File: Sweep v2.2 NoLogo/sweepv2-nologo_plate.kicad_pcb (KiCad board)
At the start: 2 copper layers, 105 x 86.9 mm, 17 parts, among them SW10 SW_Push, SW11 SW_Push, SW12 SW_Push, SW14 SW_Push, SW15 SW_Push, SW16 SW_Push, SW17 SW_Push, SW18 SW_Push, SW2 SW_Push, SW20 SW_Push, SW21 SW_Push, SW3 SW_Push, SW4 SW_Push, SW5 SW_Push, SW6 SW_Push, SW8 SW_Push, SW9 SW_Push

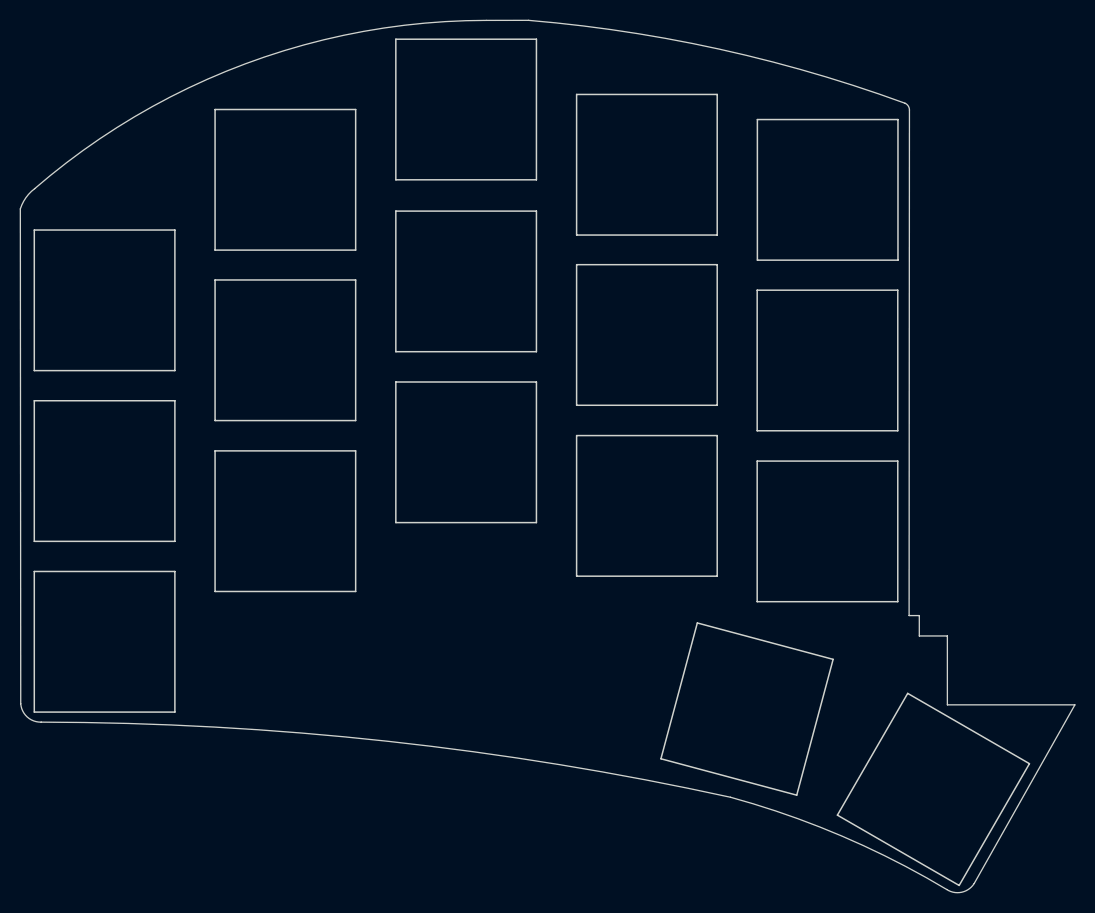
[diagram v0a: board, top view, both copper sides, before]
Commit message: chore(sweep_v2_2_nologo): update plate file format
Saving the file without any modifications resolves KiCad's complaint
about the outdated file format.
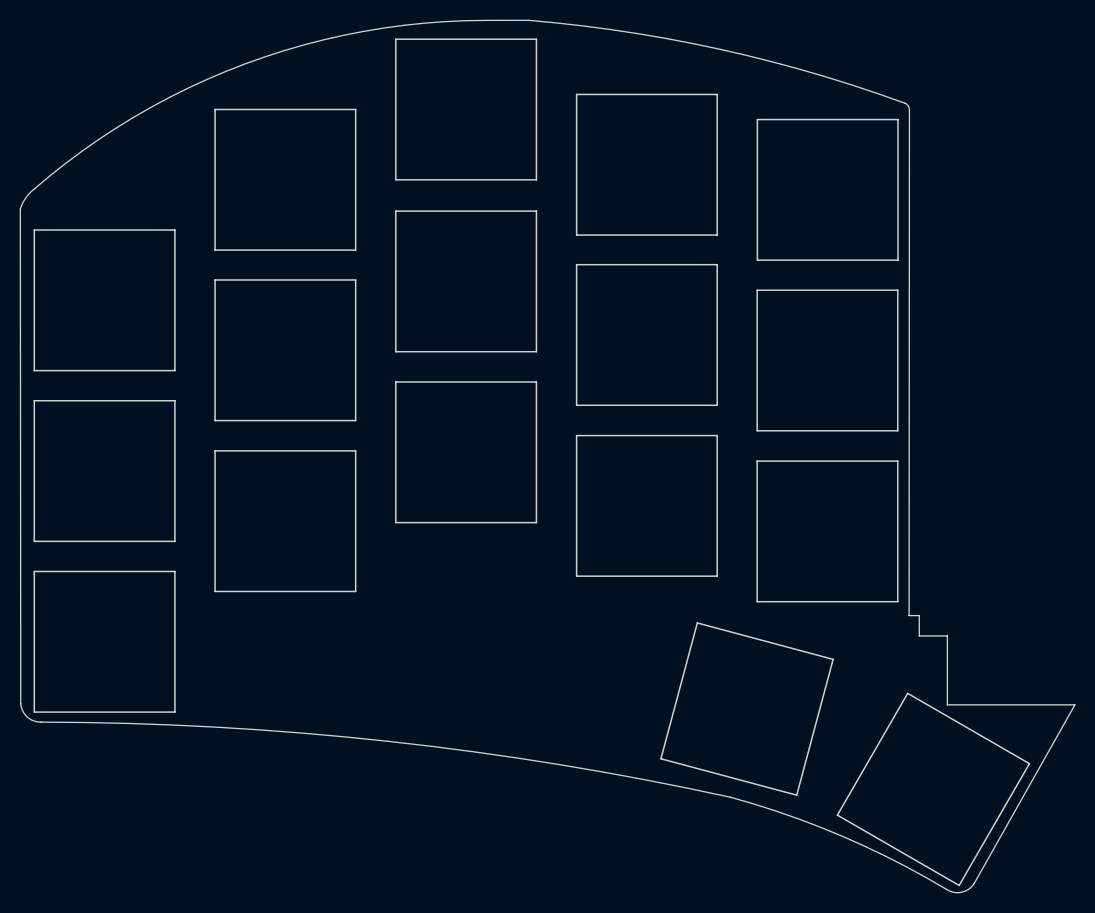
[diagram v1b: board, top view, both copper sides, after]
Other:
- net class Default removed
